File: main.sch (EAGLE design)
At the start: 26 parts, among them IC1 7805TV, IC2 L293D, U1 ATMEGA328P_TQFP

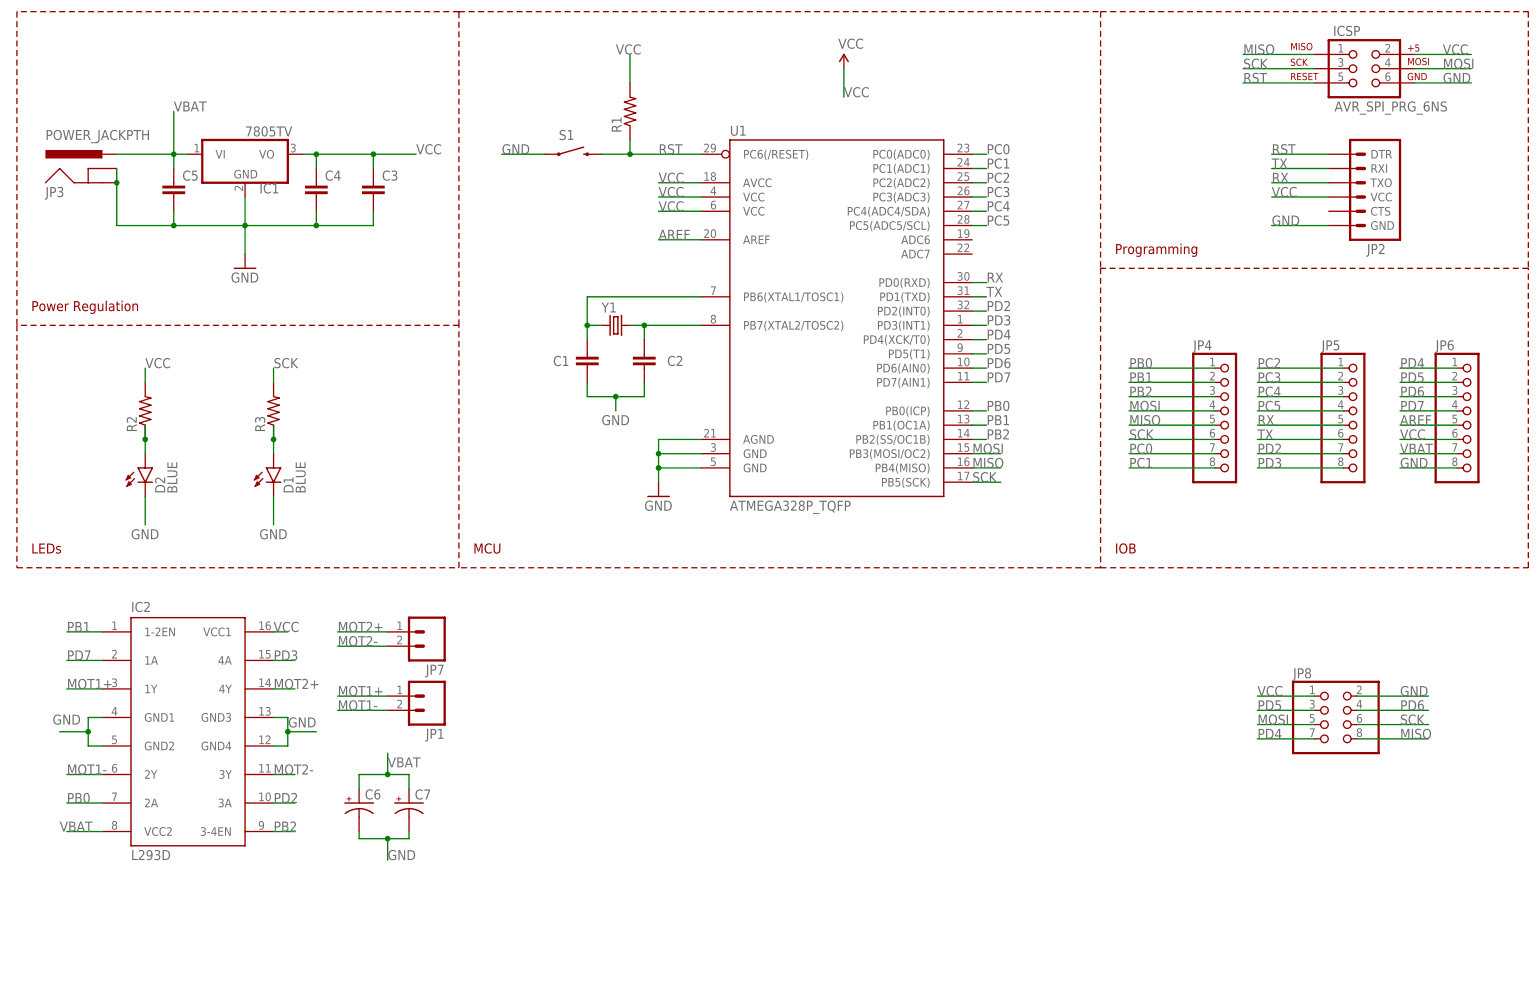
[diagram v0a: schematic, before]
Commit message: Work in progress commit for r1.1
1. Changed VREG to smaller package
2. Added RST decoupling capacitor
3. Added idiot diode
4. Removed motor controller and support circuitry.
5. Added additional decoupling capacitor
6. Reworked board outline
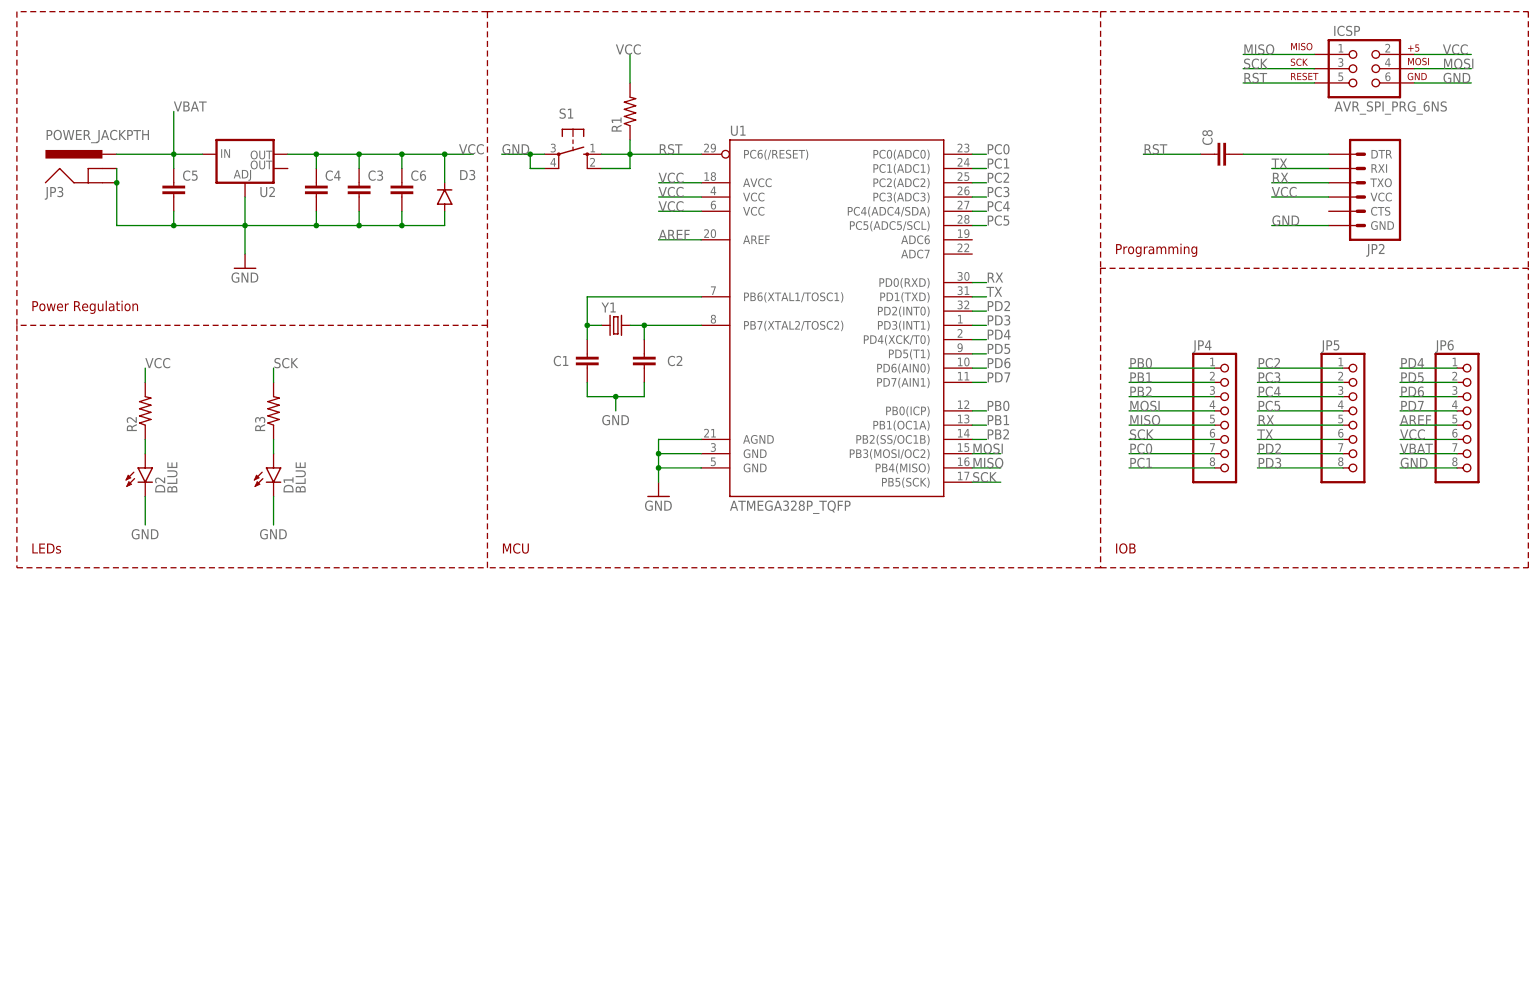
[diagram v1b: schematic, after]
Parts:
- removed C7: (no value), SparkFun-Passives:CAP_POLPTH2
- removed IC1: 7805TV, linear:7805TV
- removed IC2: L293D, st-microelectronics:L293D
- removed JP1, JP7: (no value), SparkFun-Connectors:M025MM
- removed JP8: (no value), pinhead:PINHD-2X4
- added C8: (no value), SparkFun-Passives:CAP0805
- added D3: 250mA/100V, SparkFun-DiscreteSemi:DIODEBAS16
- added U2: (no value), SparkFun-PowerIC:V_REG_LM1117SOT223
- C6: device SparkFun-Passives:CAP_POLPTH2 -> SparkFun-Passives:CAP0805
- S1: value SWITCH-MOMENTARY-2SMD -> (none); device SparkFun-Electromechanical:SWITCH-MOMENTARY-2SMD -> switch-omron:10-XX
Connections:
- net N$1 renamed XTAL_P
- net N$2 renamed XTAL_N
- removed net MOT1+: IC2.1Y, JP1.1
- removed net MOT1-: IC2.2Y, JP1.2
- removed net MOT2+: IC2.4Y, JP7.1
- removed net MOT2-: IC2.3Y, JP7.2
- new net N$5: C8.2, JP2.DTR
- net GND: now also C6.2, D3.A, S1.P, S1.P1, U2.ADJ; no longer C6.-, C7.-, IC1.GND, IC2.GND1, IC2.GND2, IC2.GND3, IC2.GND4, JP8.2, S1.1
- net MISO: no longer JP8.8
- net MOSI: no longer JP8.5
- net PB0: no longer IC2.2A
- net PB1: no longer IC2.1-2EN
- net PB2: no longer IC2.3-4EN
- net PD2: no longer IC2.3A
- net PD3: no longer IC2.4A
- net PD4: no longer JP8.7
- net PD5: no longer JP8.3
- net PD6: no longer JP8.4
- net PD7: no longer IC2.1A
- net RST: now also C8.1, S1.S, S1.S1; no longer JP2.DTR, S1.2
- net SCK: no longer JP8.6
- net VBAT: now also U2.IN; no longer C6.+, C7.+, IC1.VI, IC2.VCC2
- net VCC: now also C6.1, D3.C, U2.OUT; no longer IC1.VO, IC2.VCC1, JP8.1
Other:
- moved on the sheet: C3

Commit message: Added UART-USB Chip
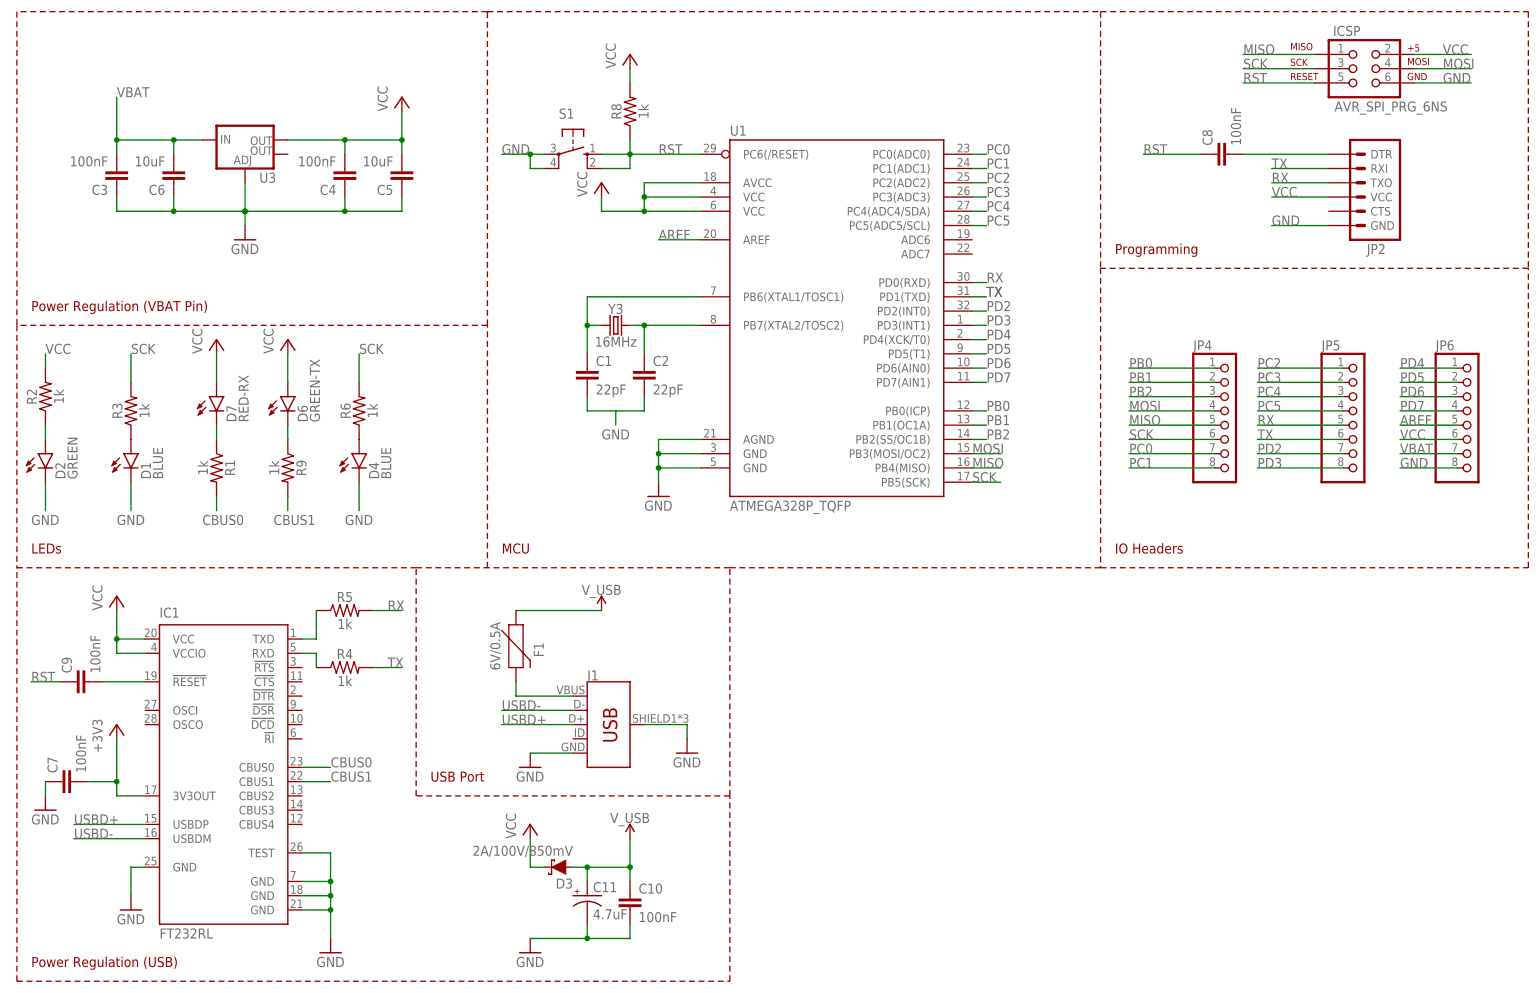
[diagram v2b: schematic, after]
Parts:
- removed JP3: POWER_JACKPTH, SparkFun-Connectors:POWER_JACKPTH
- removed U2: (no value), SparkFun-PowerIC:V_REG_LM1117SOT223
- removed Y1: (no value), SparkFun-FreqCtrl:CRYSTALHC49US
- added C10, C7, C9: 100nF, SparkFun-Capacitors:0.1UF-0603-25V-5%
- added C11: 4.7uF, SparkFun-Capacitors:10UF-POLAR-0603-6.3V-20%(TANT)
- added D4: BLUE, SparkFun-LED:LED-BLUE0603
- added D6: GREEN-TX, SparkFun-LED:LED-BLUE0603
- added D7: RED-RX, SparkFun-LED:LED-BLUE0603
- added F1: 6V/0.5A, SparkFun-Fuses:PPTC_HALF-AMP
- added IC1: FT232RL, ftdichip:FT232RL
- added J1: (no value), SparkFun-Connectors:USB_MICRO-B_FEMALE-SMT
- added R4, R5, R6, R8, R9: 1k, SparkFun-Resistors:RESISTOR0805
- added U3: (no value), SparkFun-IC-Power:V_REG_LM1117SOT223
- added Y3: 16MHz, SparkFun-Clocks:CRYSTAL-16MHZPTH-HC49US
- C1, C2: value (none) -> 22pF
- C3, C4, C8: value (none) -> 100nF; device SparkFun-Passives:CAP0805 -> SparkFun-Capacitors:0.1UF-0603-25V-5%
- C5, C6: value (none) -> 10uF; device SparkFun-Passives:CAP0805 -> SparkFun-Capacitors:0.1UF-0603-25V-5%
- D2: value BLUE -> GREEN
- D3: value 250mA/100V -> 2A/100V/850mV; device SparkFun-DiscreteSemi:DIODEBAS16 -> SparkFun-DiscreteSemi:DIODE-SCHOTTKY-SS14
- R1, R2, R3: value (none) -> 1k; device SparkFun-Resistors:RESISTOR0805-RES -> SparkFun-Resistors:RESISTOR0805
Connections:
- new net +3V3: C7.2, IC1.3V3OUT
- new net CBUS0: IC1.CBUS0, R1.2
- new net CBUS1: IC1.CBUS1, R9.2
- new net N$1: IC1.TXD, R5.1
- new net N$10: F1.2, J1.VBUS
- new net N$13: D7.C, R1.1
- new net N$14: D6.C, R9.1
- new net N$15: IC1.USBDM
- new net N$16: IC1.USBDP
- new net N$2: IC1.RXD, R4.1
- new net N$6: D4.A, R6.1
- new net N$7: C9.2, IC1.!RESET
- new net N$8: C1.2, C2.2
- new net USBD+: J1.D+
- new net USBD-: J1.D-
- new net V_USB: C10.1, C11.+, D3.A, F1.1
- net GND: now also C10.2, C11.-, C3.1, C4.1, C5.1, C6.1, C7.1, D4.C, IC1.GND, IC1.GND@1, IC1.GND@2, IC1.GND@A, IC1.TEST, J1.GND, J1.SHIELD, U3.ADJ; no longer C1.2, C2.2, C3.2, C4.2, C5.2, C6.2, D3.A, JP3.GND, JP3.GNDBREAK, U2.ADJ
- net RST: now also C9.1, R8.1; no longer R1.1
- net RX: now also R5.2
- net SCK: now also R6.2
- net TX: now also R4.2
- net VBAT: now also C3.2, C6.2, U3.IN; no longer C5.1, JP3.PWR, U2.IN
- net VCC: now also C4.2, C5.2, D6.A, D7.A, IC1.VCC, IC1.VCCIO, R8.2, U3.OUT; no longer C3.1, C4.1, C6.1, R1.2, U2.OUT
- net XTAL_N: now also Y3.2; no longer Y1.1
- net XTAL_P: now also Y3.1; no longer Y1.2
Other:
- note added: "IO Headers"
- note added: "Power Regulation (USB)"
- note added: "Power Regulation (VBAT Pin)"
- note added: "USB Port"
- note removed: "IOB"
- note removed: "Power Regulation"
- moved on the sheet: C1, C2, C3, C4, C5, C6, D1, D2, R1, R2, R3

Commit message: Board layout made
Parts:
- removed C1: 22pF, SparkFun-Passives:CAP0805
- removed C10, C3, C8, C9: 100nF, SparkFun-Capacitors:0.1UF-0603-25V-5%
- removed D2: GREEN, SparkFun-LED:LED-BLUE0603
- removed D6: GREEN-TX, SparkFun-LED:LED-BLUE0603
- removed R1, R6, R9: 1k, SparkFun-Resistors:RESISTOR0805
- removed U3: (no value), SparkFun-IC-Power:V_REG_LM1117SOT223
- added R7: 1k, SparkFun-Resistors:RESISTOR0805
- C2: value 22pF -> 0.1uF; device SparkFun-Passives:CAP0805 -> SparkFun-Capacitors:0.1UF-0603-25V-5%
- C4: value 100nF -> 22pF; device SparkFun-Capacitors:0.1UF-0603-25V-5% -> SparkFun-Capacitors:22PF-0603-50V-5%
- C5: value 10uF -> 22pF; device SparkFun-Capacitors:0.1UF-0603-25V-5% -> SparkFun-Capacitors:22PF-0603-50V-5%
- C6: value 10uF -> 0.1uF
- C7: value 100nF -> 0.1uF
- D4: value BLUE -> RED; device SparkFun-LED:LED-BLUE0603 -> SparkFun-LED:LED-RED0603
- D7: value RED-RX -> GREEN; device SparkFun-LED:LED-BLUE0603 -> SparkFun-LED:LED-GREEN0603
- U1: device SparkFun-DigitalIC:ATMEGA328P_TQFP -> SparkFun-IC-Microcontroller:ATMEGA328P_TQFP
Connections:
- net N$10 renamed VBUS
- removed net +3V3: C7.2, IC1.3V3OUT
- removed net N$1: IC1.TXD, R5.1
- removed net N$13: D7.C, R1.1
- removed net N$14: D6.C, R9.1
- removed net N$16: IC1.USBDP
- removed net N$2: IC1.RXD, R4.1
- removed net N$4: D1.A, R3.1
- removed net N$5: C8.2, JP2.DTR
- removed net N$6: D4.A, R6.1
- removed net N$8: C1.2, C2.2
- new net 3.3V: C6.2, IC1.3V3OUT
- new net 5V: D1.A, D3.C, D4.A, R2.2, R3.2, R7.2, R8.2
- new net N$17: U1.AGND, U1.GND@3, U1.GND@5
- new net N$19: J1.GND
- new net N$20: J1.SHIELD
- new net N$21: IC1.GND, IC1.GND@1, IC1.GND@2, IC1.TEST
- new net N$22: IC1.GND@A
- net CBUS0: now also R2.1; no longer R1.2
- net CBUS1: now also R3.1; no longer R9.2
- net GND: now also D7.C; no longer C10.2, C3.1, D1.C, D2.C, D4.C, IC1.GND, IC1.GND@1, IC1.GND@2, IC1.GND@A, IC1.TEST, J1.GND, J1.SHIELD, U1.AGND, U1.GND@3, U1.GND@5, U3.ADJ
- net N$15: now also IC1.VCC, IC1.VCCIO; no longer IC1.USBDM
- net N$3: now also D7.A, R7.1; no longer D2.A, R2.1
- net N$7: now also C2.2; no longer C9.2
- net RST: now also C2.1, JP2.DTR; no longer C8.1, C9.1
- net RX: now also D1.C, IC1.TXD, R4.1, R4.2; no longer R5.2
- net SCK: no longer R3.2, R6.2
- net TX: now also D4.C, IC1.RXD, R5.1, R5.2; no longer R4.2
- net USBD+: now also IC1.USBDP
- net USBD-: now also IC1.USBDM
- net VBAT: no longer C3.2, C6.2, U3.IN
- net VCC: no longer C4.2, C5.2, D3.C, D6.A, D7.A, IC1.VCC, IC1.VCCIO, R2.2, R8.2, U3.OUT
- net V_USB: now also C7.2; no longer C10.1
- net XTAL_N: now also C5.2; no longer C2.1
- net XTAL_P: now also C4.2; no longer C1.1
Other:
- moved on the sheet: C11, C2, C4, C5, C6, C7, D3, R2, R3, R4, R5, Y3

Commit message: Diff lines routed
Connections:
- net USBD+ renamed USBD_P
- net USBD- renamed USBD_N
- removed net N$15: IC1.VCC, IC1.VCCIO
- removed net N$17: U1.AGND, U1.GND@3, U1.GND@5
- removed net N$19: J1.GND
- removed net N$20: J1.SHIELD
- removed net N$21: IC1.GND, IC1.GND@1, IC1.GND@2, IC1.TEST
- removed net N$22: IC1.GND@A
- removed net VBAT: JP6.7
- net 5V: now also IC1.VCC, IC1.VCCIO
- net GND: now also IC1.GND, IC1.GND@1, IC1.GND@2, IC1.GND@A, IC1.TEST, J1.GND, J1.SHIELD, U1.AGND, U1.GND@3, U1.GND@5
- net RX: now also IC1.RXD, R5.2
- net TX: no longer IC1.RXD, R5.2
